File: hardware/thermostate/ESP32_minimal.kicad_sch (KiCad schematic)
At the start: 28 parts, among them IC1 L8050QLT1G, IC2 L8050QLT1G, P1 USB_C_Plug_USB2.0, SW1 SW_Push, SW2 SW_Push, U1 ESP32-S3-WROOM-1, U2 LM1117-3.3

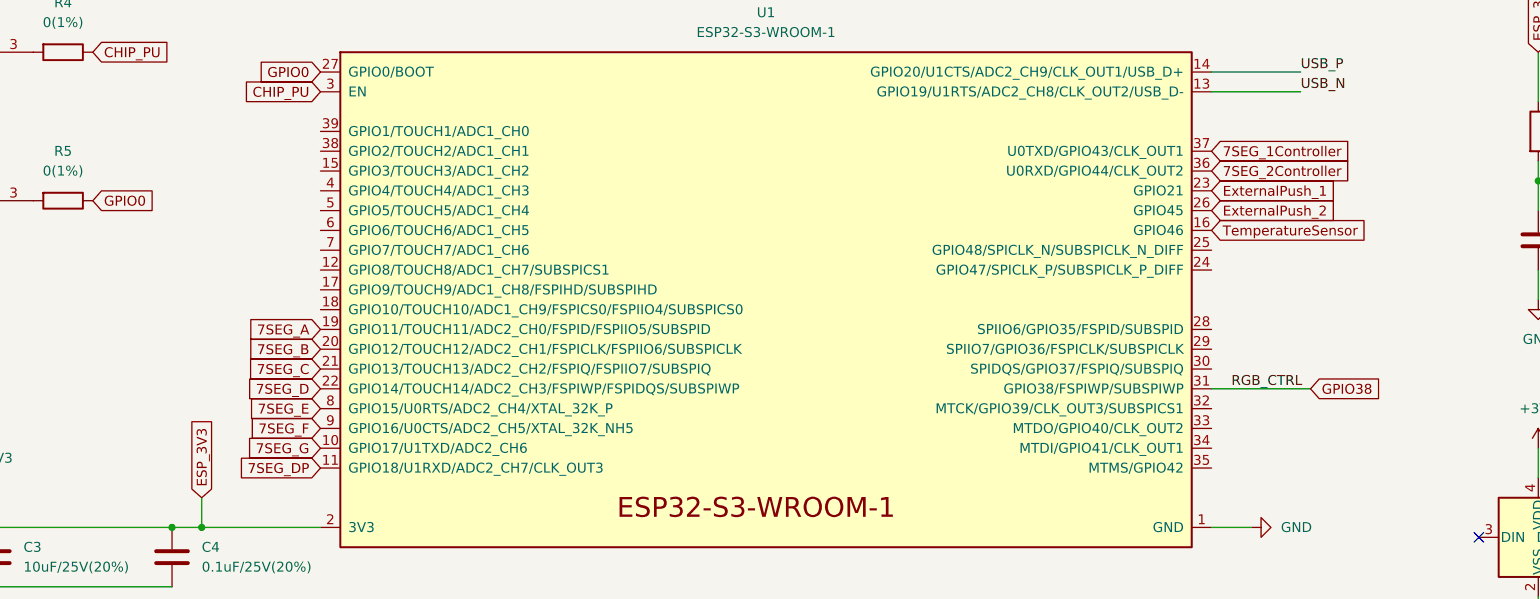
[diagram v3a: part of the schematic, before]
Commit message: Add First lines PCB
Signed-off-by: Javier <javierfernandezvillasante@gmail.com>
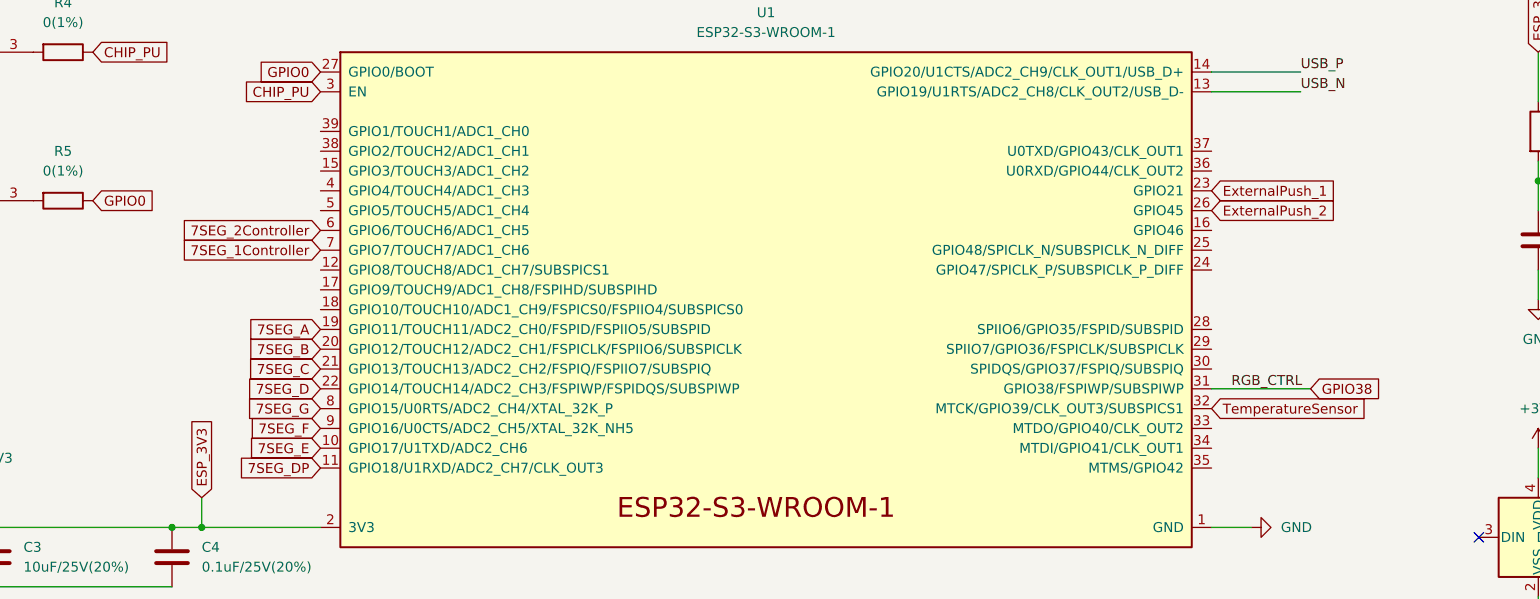
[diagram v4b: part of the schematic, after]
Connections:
- net 7SEG_1Controller: now also U1.7 (GPIO7/TOUCH7/ADC1_CH6); no longer U1.37 (U0TXD/GPIO43/CLK_OUT1)
- net 7SEG_2Controller: now also U1.6 (GPIO6/TOUCH6/ADC1_CH5); no longer U1.36 (U0RXD/GPIO44/CLK_OUT2)
- net 7SEG_E: now also U1.10 (GPIO17/U1TXD/ADC2_CH6); no longer U1.8 (GPIO15/U0RTS/ADC2_CH4/XTAL_32K_P)
- net 7SEG_G: now also U1.8 (GPIO15/U0RTS/ADC2_CH4/XTAL_32K_P); no longer U1.10 (GPIO17/U1TXD/ADC2_CH6)
- net TemperatureSensor: now also U1.32 (MTCK/GPIO39/CLK_OUT3/SUBSPICS1); no longer U1.16 (GPIO46)
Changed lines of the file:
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@@
+    )
+  )
+  (global_label "TemperatureSensor" (shape input) (at 214.63 76.2 0) (fields_autoplaced)
+    (effects (font (size 1.27 1.27)) (justify left))
+    (property "Intersheet References" "${INTERSHEET_REFS}" (id 0) (at 235.1255 76.1206 0)
+      (effects (font (size 1.27 1.27)) (justify left) hide)
     )
   )
@@
     )
   )
-  (global_label "7SEG_2Controller" (shape input) (at 214.63 45.72 0) (fields_autoplaced)
-    (effects (font (size 1.27 1.27)) (justify left))
-    (property "Intersheet References" "${INTERSHEET_REFS}" (id 0) (at 233.4926 45.7994 0)
-      (effects (font (size 1.27 1.27)) (justify left) hide)
-    )
-  )
   (global_label "7SEG_D" (shape input) (at 100.33 73.66 180) (fields_autoplaced)
     (effects (font (size 1.27 1.27)) (justify right))
     (property "Intersheet References" "${INTERSHEET_REFS}" (id 0) (at 90.8412 73.5806 0)
+      (effects (font (size 1.27 1.27)) (justify right) hide)
+    )
+  )
+  (global_label "7SEG_F" (shape input) (at 100.33 78.74 180) (fields_autoplaced)
+    (effects (font (size 1.27 1.27)) (justify right))
+    (property "Intersheet References" "${INTERSHEET_REFS}" (id 0) (at 91.0226 78.6606 0)
+      (effects (font (size 1.27 1.27)) (justify right) hide)
+    )
+  )
+  (global_label "7SEG_2Controller" (shape input) (at 100.33 53.34 180) (fields_autoplaced)
+    (effects (font (size 1.27 1.27)) (justify right))
+    (property "Intersheet References" "${INTERSHEET_REFS}" (id 0) (at 81.4674 53.2606 0)
       (effects (font (size 1.27 1.27)) (justify right) hide)
     )
@@
     )
   )
-  (global_label "TemperatureSensor" (shape input) (at 214.63 53.34 0) (fields_autoplaced)
-    (effects (font (size 1.27 1.27)) (justify left))
-    (property "Intersheet References" "${INTERSHEET_REFS}" (id 0) (at 235.1255 53.2606 0)
-      (effects (font (size 1.27 1.27)) (justify left) hide)
-    )
-  )
   (global_label "ExternalPush_2" (shape input) (at 214.63 50.8 0) (fields_autoplaced)
     (effects (font (size 1.27 1.27)) (justify left))
     (property "Intersheet References" "${INTERSHEET_REFS}" (id 0) (at 231.5574 50.7206 0)
       (effects (font (size 1.27 1.27)) (justify left) hide)
-    )
-  )
-  (global_label "7SEG_F" (shape input) (at 100.33 78.74 180) (fields_autoplaced)
-    (effects (font (size 1.27 1.27)) (justify right))
-    (property "Intersheet References" "${INTERSHEET_REFS}" (id 0) (at 91.0226 78.6606 0)
-      (effects (font (size 1.27 1.27)) (justify right) hide)
     )
   )
@@
     (effects (font (size 1.27 1.27)) (justify right))
     (property "Intersheet References" "${INTERSHEET_REFS}" (id 0) (at 91.0226 65.9606 0)
-      (effects (font (size 1.27 1.27)) (justify right) hide)
-    )
-  )
-  (global_label "7SEG_1Controller" (shape input) (at 214.63 43.18 0) (fields_autoplaced)
-    (effects (font (size 1.27 1.27)) (justify left))
-    (property "Intersheet References" "${INTERSHEET_REFS}" (id 0) (at 233.4926 43.2594 0)
-      (effects (font (size 1.27 1.27)) (justify left) hide)
-    )
-  )
-  (global_label "7SEG_E" (shape input) (at 100.33 76.2 180) (fields_autoplaced)
-    (effects (font (size 1.27 1.27)) (justify right))
-    (property "Intersheet References" "${INTERSHEET_REFS}" (id 0) (at 90.9621 76.1206 0)
       (effects (font (size 1.27 1.27)) (justify right) hide)
     )
@@
     (property "Intersheet References" "${INTERSHEET_REFS}" (id 0) (at 236.6374 73.5806 0)
       (effects (font (size 1.27 1.27)) (justify left) hide)
+    )
+  )
+  (global_label "7SEG_1Controller" (shape input) (at 100.33 55.88 180) (fields_autoplaced)
+    (effects (font (size 1.27 1.27)) (justify right))
+    (property "Intersheet References" "${INTERSHEET_REFS}" (id 0) (at 81.4674 55.8006 0)
+      (effects (font (size 1.27 1.27)) (justify right) hide)
     )
   )
@@
     )
   )
+  (global_label "7SEG_E" (shape input) (at 100.33 81.28 180) (fields_autoplaced)
+    (effects (font (size 1.27 1.27)) (justify right))
+    (property "Intersheet References" "${INTERSHEET_REFS}" (id 0) (at 90.9621 81.2006 0)
+      (effects (font (size 1.27 1.27)) (justify right) hide)
+    )
+  )
   (global_label "DTR" (shape input) (at 19.05 30.48 180) (fields_autoplaced)
     (effects (font (size 1.27 1.27)) (justify right))
@@
     )
   )
-  (global_label "7SEG_G" (shape input) (at 100.33 81.28 180) (fields_autoplaced)
+  (global_label "7SEG_G" (shape input) (at 100.33 76.2 180) (fields_autoplaced)
     (effects (font (size 1.27 1.27)) (justify right))
-    (property "Intersheet References" "${INTERSHEET_REFS}" (id 0) (at 90.8412 81.2006 0)
+    (property "Intersheet References" "${INTERSHEET_REFS}" (id 0) (at 90.8412 76.1206 0)
       (effects (font (size 1.27 1.27)) (justify right) hide)
     )

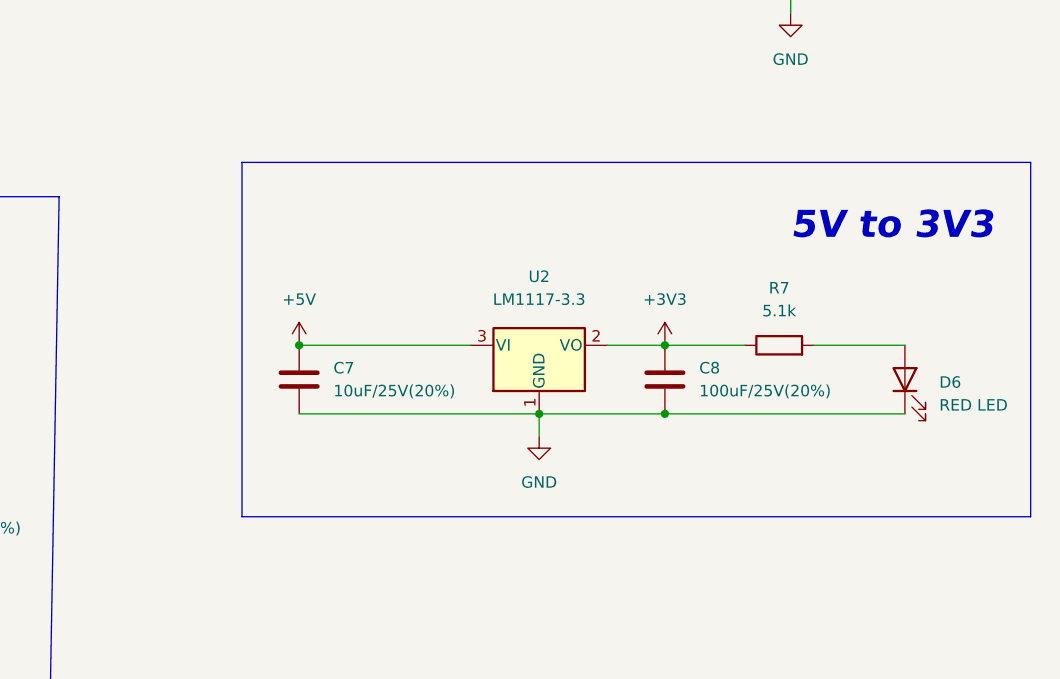
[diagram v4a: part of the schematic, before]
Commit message: Add SCH with low power components
Signed-off-by: Javier <javierfernandezvillasante@gmail.com>
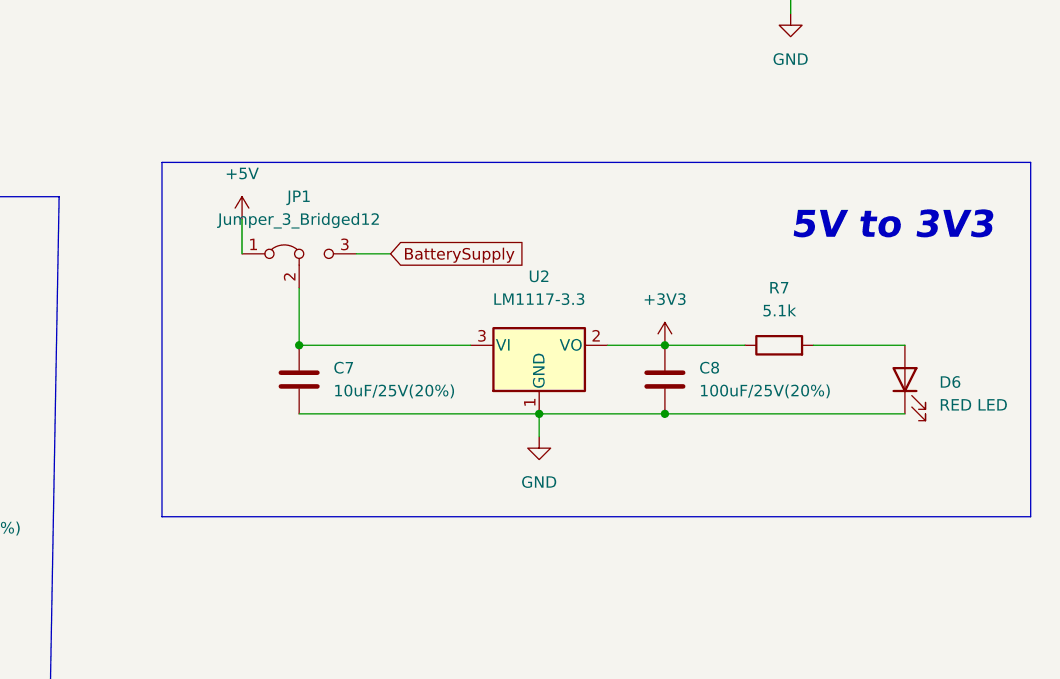
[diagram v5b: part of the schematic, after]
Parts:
- added JP1: Jumper_3_Bridged12, Jumper:SolderJumper-3_P2.0mm_Open_TrianglePad1.0x1.5mm, symbol Jumper:Jumper_3_Bridged12
- P1: footprint Connector_USB:USB_C_Receptacle_Amphenol_12401610E4-2A -> Connector_USB:USB_C_Receptacle_G-Switch_GT-USB-7010ASV
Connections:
- net +5V: now also JP1.1 (A); no longer C7.1, U2.3 (VI)
- new net: C7.1, JP1.2 (C), U2.3 (VI)
- new net BatterySupply: JP1.3 (B)

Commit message: Stop until next winter
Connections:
- net RelayControlSignal: now reaches U1.16 (GPIO46)
- net Potenciometro: now reaches U1.18 (GPIO10/TOUCH10/ADC1_CH9/FSPICS0/FSPIIO4/SUBSPICS0)
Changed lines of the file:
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@@
+    )
+  )
+  (global_label "Potenciometro" (shape input) (at 100.33 63.5 180) (fields_autoplaced)
+    (effects (font (size 1.27 1.27)) (justify right))
+    (property "Intersheet References" "${INTERSHEET_REFS}" (id 0) (at 84.2493 63.4206 0)
+      (effects (font (size 1.27 1.27)) (justify right) hide)
     )
   )
@@
     )
   )
+  (global_label "RelayControlSignal" (shape input) (at 214.63 53.34 0) (fields_autoplaced)
+    (effects (font (size 1.27 1.27)) (justify left))
+    (property "Intersheet References" "${INTERSHEET_REFS}" (id 0) (at 235.0045 53.2606 0)
+      (effects (font (size 1.27 1.27)) (justify left) hide)
+    )
+  )
